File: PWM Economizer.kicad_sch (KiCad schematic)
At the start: 2 parts, among them U10 DRV110A

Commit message: More schematic completed
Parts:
- added C13: 330nF, symbol Device:C_Small
- added J6: Conn_01x02, symbol Connector_Generic:Conn_01x02
- added Q3: FDMS86255, Package_TO_SOT_SMD:TDSON-8-1, symbol Transistor_FET:FDMS86255
- added R18, R21, R25: R_Small, symbol Device:R_Small
- added R23: 1R, symbol Device:R_Small
- added U12: AQY212, Package_SO:SOP-4_3.8x4.1mm_P2.54mm, symbol Relay_SolidState:TLP175A
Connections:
- net GND: now also U10.3 (OSC), C13.2, R21.2, R23.2, R25.1
- net at U10.1 (KEEP): now also C13.1
- net at U10.2 (PEAK): now also R21.1
- net at U10.6 (SENSE): now also Q3.1 (S), Q3.2 (S), Q3.3 (S), R23.1
- net at U10.7 (OUT): now also Q3.4 (G)
- net +5V: no longer names the net of C11.1, U10.4 (VIN)
- net +5V: now also R18.1
- new net: J6.1 (Pin_1), R18.2, U12.3
- new net: R25.2, U12.2
- new net: J6.2 (Pin_2), Q3.5 (D)
- new net Control: U12.1
- new net Shutdown Loop: U12.4
- no-connect marks 0 -> 1
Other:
- note added: "Default Enabled"
- note added: "Likeley oversized. need 400mA"
- note added: "Supply capacitor for inrush max 250ms"
- moved on the sheet: C11

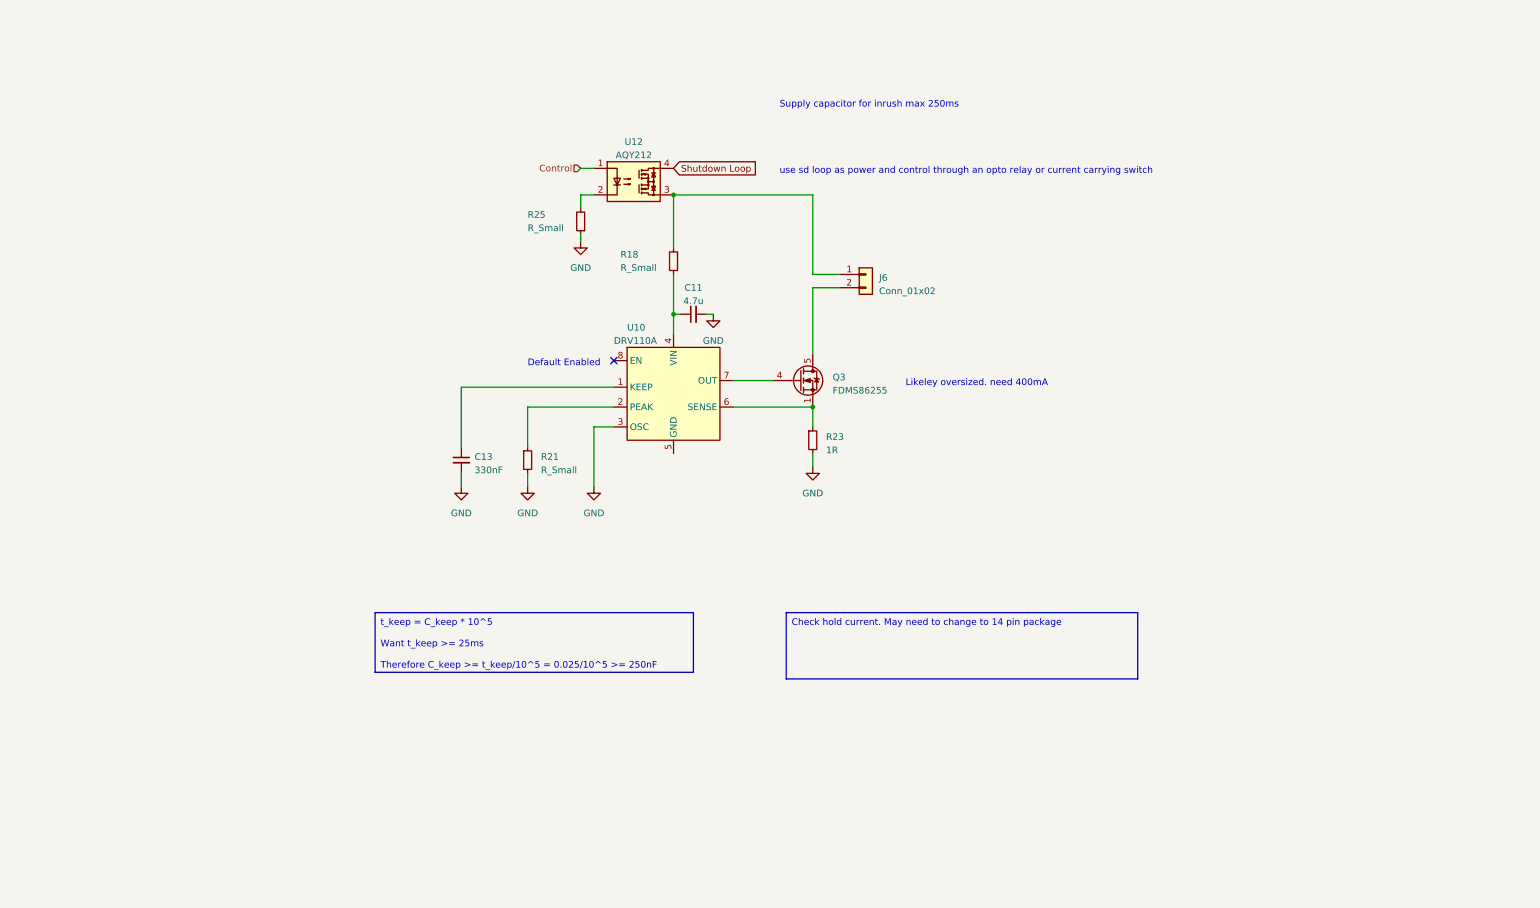
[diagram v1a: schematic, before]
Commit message: Changed to DRV110A
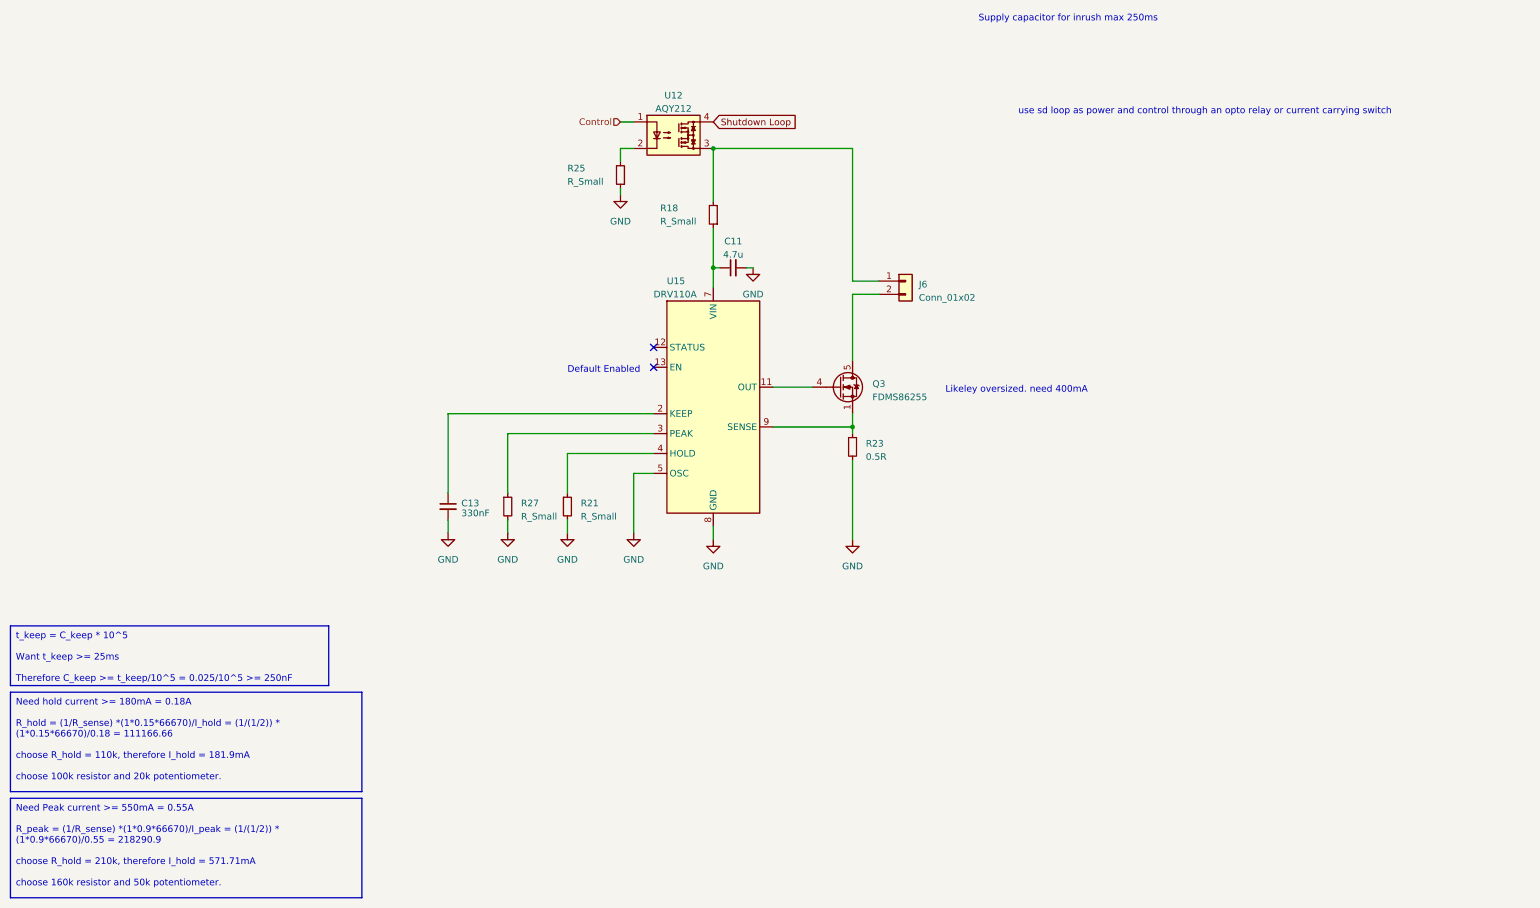
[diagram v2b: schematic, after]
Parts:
- removed U10: DRV110A, Package_SO:TSSOP-8_4.4x3mm_P0.65mm, symbol UCM:DRV110
- added R27: R_Small, symbol Device:R_Small
- added U15: DRV110A, Package_SO:TSSOP-14_4.4x5mm_P0.65mm, symbol UCM:DRV110A
- R23: value 1R -> 0.5R
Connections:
- net GND: now also R27.2, U15.5 (OSC), U15.8 (GND)
- net at C11.1, R18.1: now also U15.7 (VIN)
- net at C13.1: now also U15.2 (KEEP)
- net at Q3.1 (S), Q3.2 (S), Q3.3 (S)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: now also U15.9 (SENSE)
- net at R21.1: now also U15.4 (HOLD)
- net at Q3.4 (G): now also U15.11 (OUT)
- new net: U15.1, U15.10, U15.14
- new net: R27.1, U15.3 (PEAK)
- no-connect marks 1 -> 2
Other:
- moved on the sheet: C11, C13, J6, Q3, R18, R21, R23, R25, U12
